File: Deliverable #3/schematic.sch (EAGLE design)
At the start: 61 parts, among them Q1 MMBT4403, Q2 MMBT4403, U1 JOYSTICKPTH, U2 HX711, U3 JOYSTICKPTH, U4 MSP430FR5994IZVW, U5 HX711, U6 VL6180V1NR/1, U7 OSHW-LOGOS

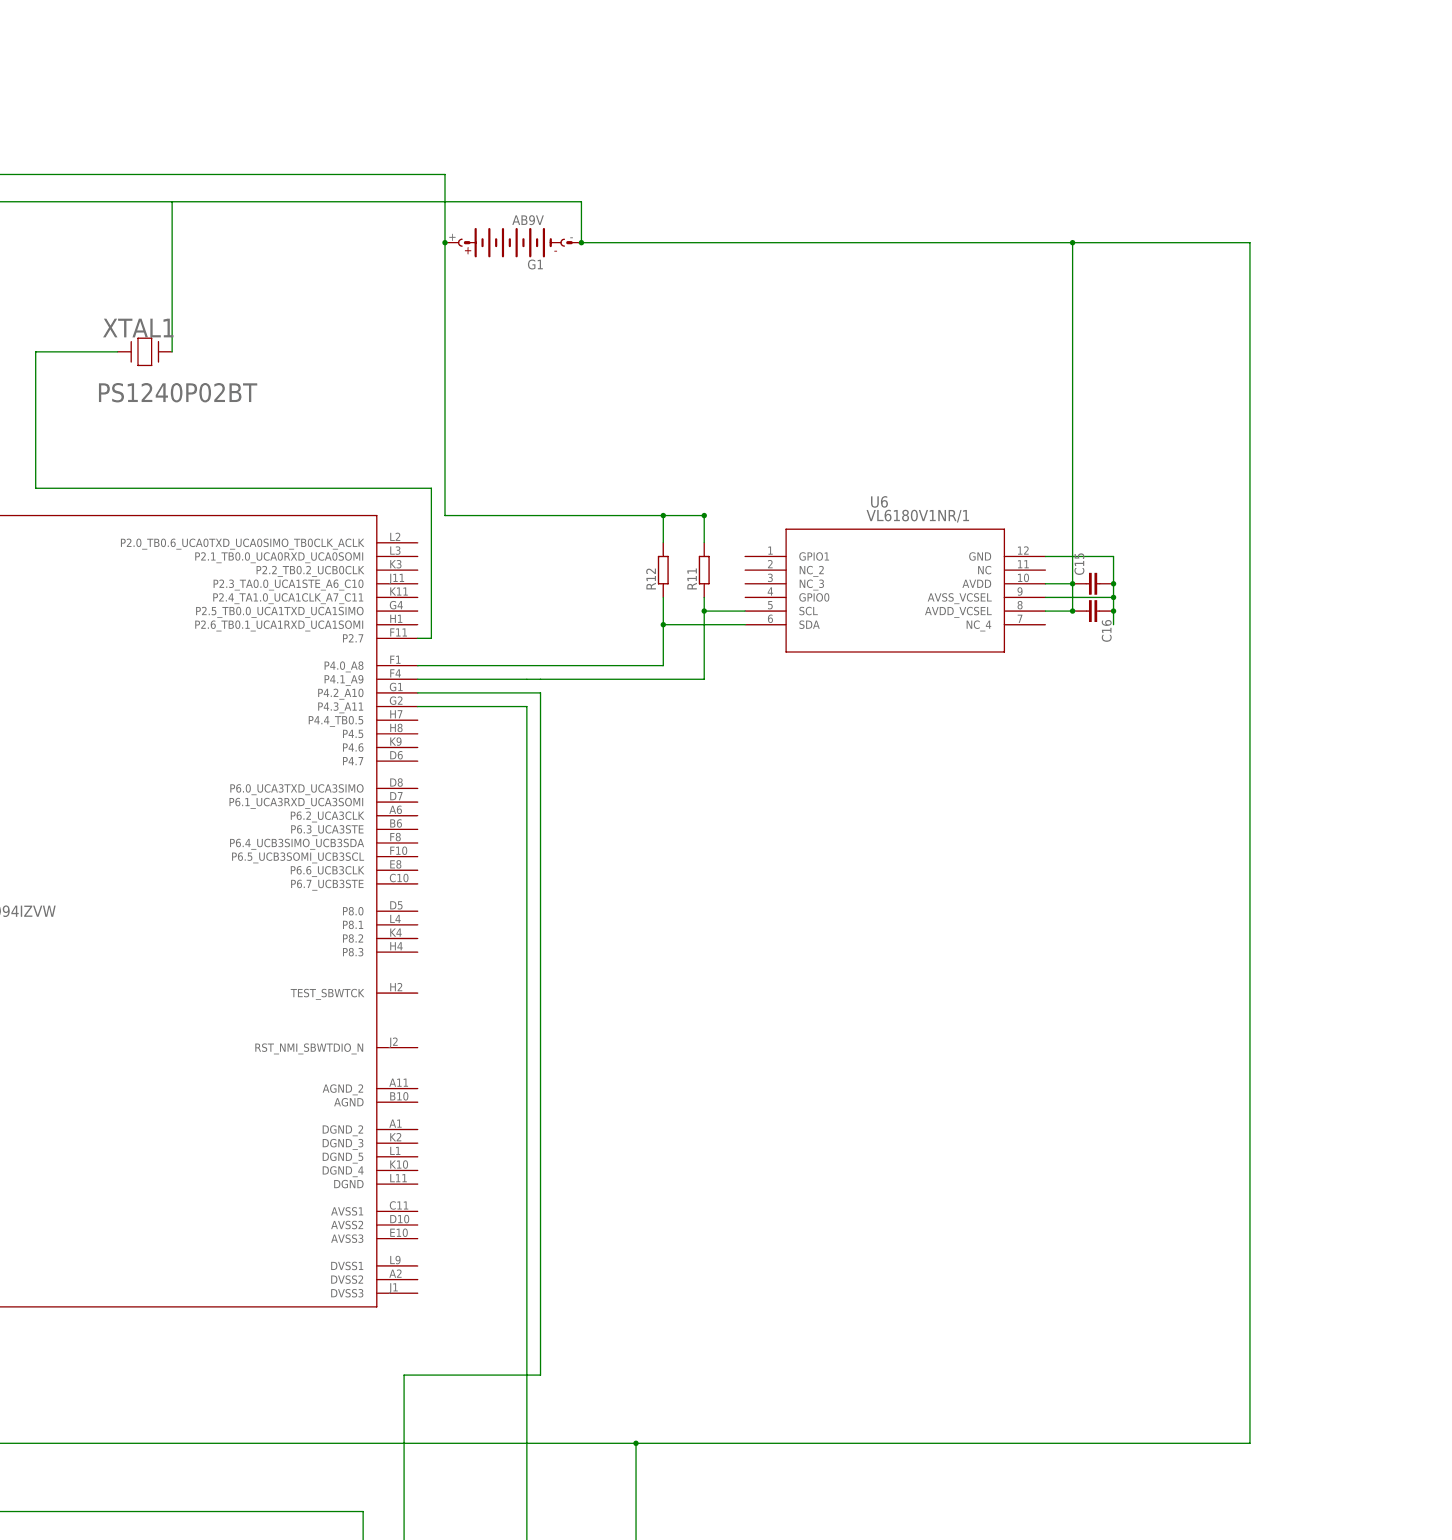
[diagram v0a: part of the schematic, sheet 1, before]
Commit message: added servo to schematic
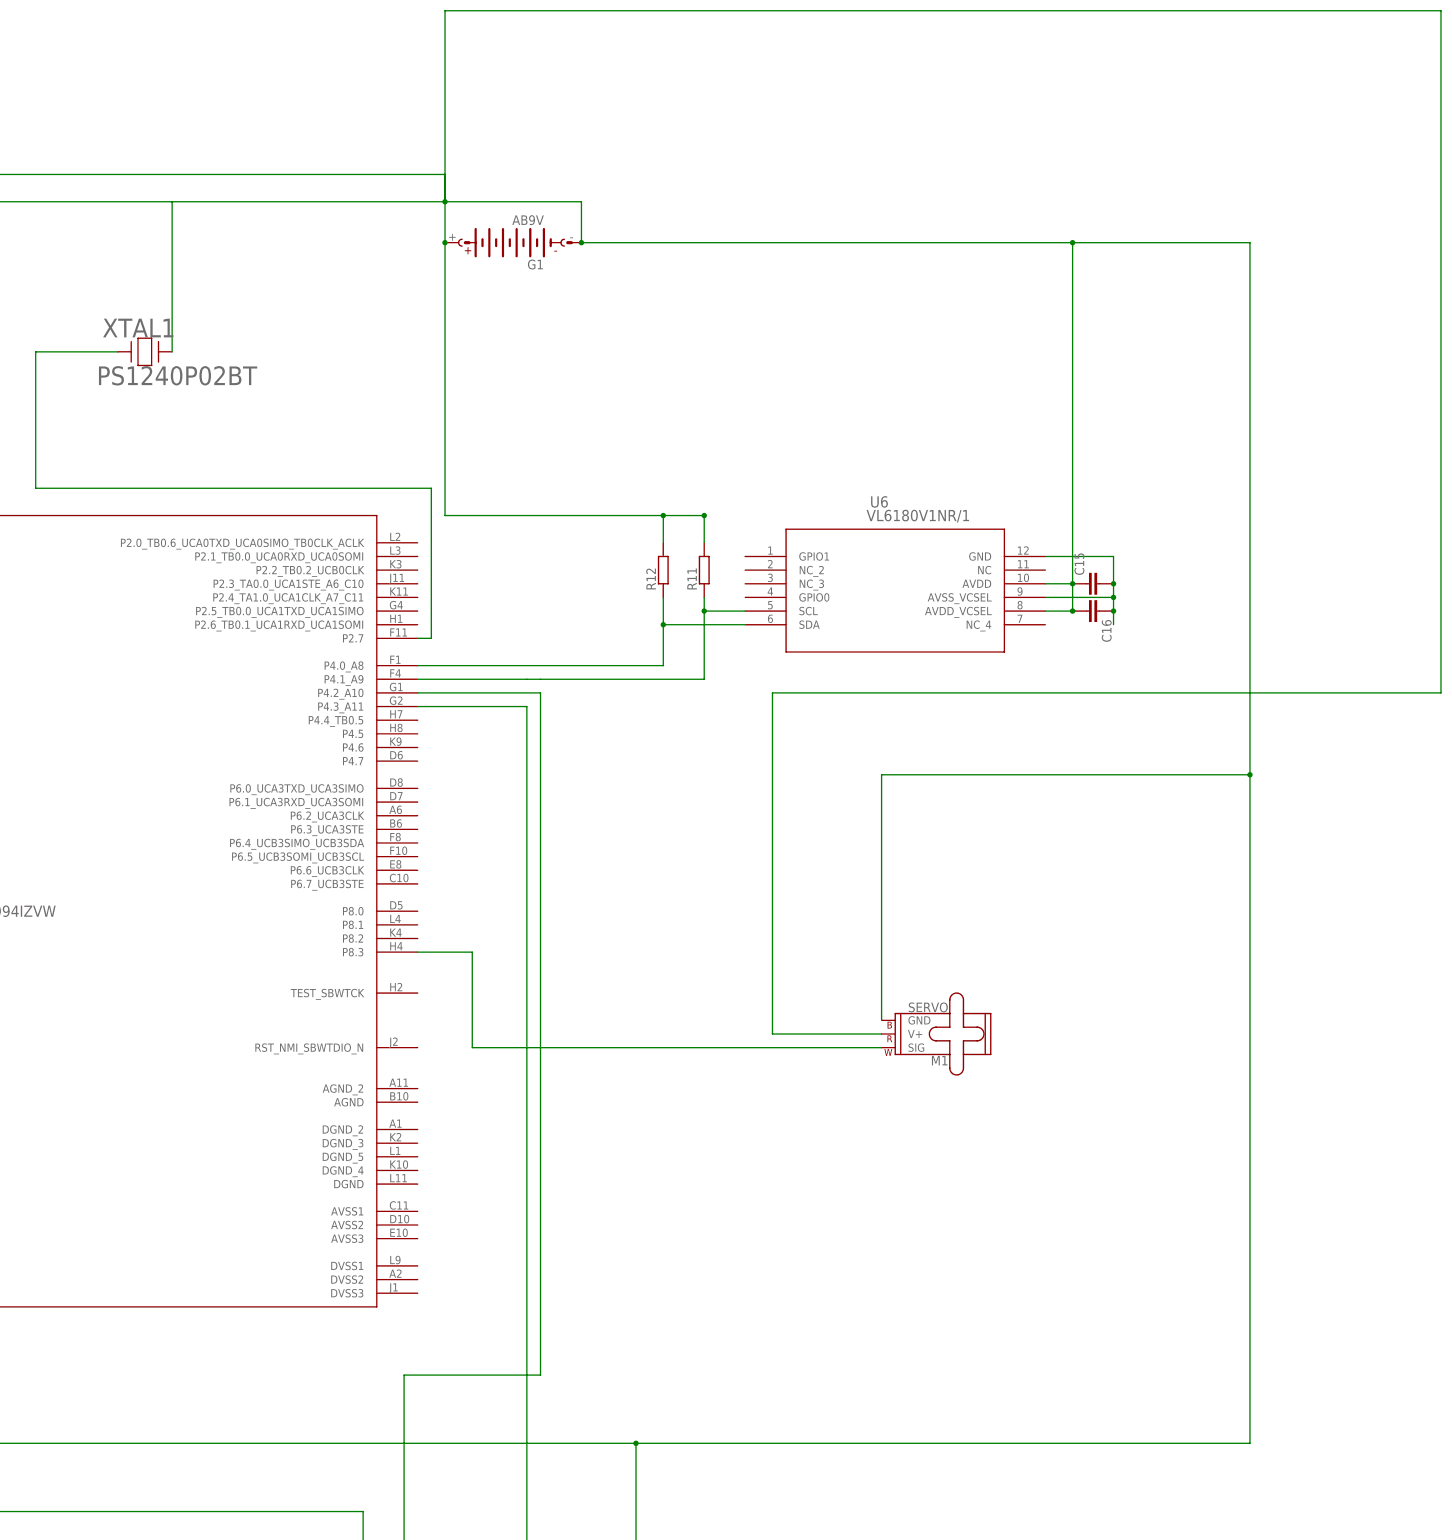
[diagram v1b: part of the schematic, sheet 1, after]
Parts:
- added M1: SERVO, SparkFun-Electromechanical:SERVO
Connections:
- new net N$13: M1.SIG, U4.P8.3
- net GND: now also M1.GND, M1.V+
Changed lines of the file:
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@@
 <layer number="115" name="ReferenceISLANDS" color="7" fill="1" visible="yes" active="yes"/>
 <layer number="116" name="Patch_BOT" color="9" fill="4" visible="yes" active="yes"/>
+<layer number="117" name="PM_Ref" color="26" fill="1" visible="no" active="no"/>
 <layer number="118" name="Rect_Pads" color="7" fill="1" visible="yes" active="yes"/>
+<layer number="119" name="PF_Ref" color="31" fill="1" visible="no" active="no"/>
+<layer number="120" name="WFL_Ref" color="25" fill="1" visible="no" active="no"/>
 <layer number="121" name="_tsilk" color="7" fill="1" visible="yes" active="yes"/>
 <layer number="122" name="_bsilk" color="7" fill="1" visible="yes" active="yes"/>
@@
 <layer number="128" name="_bValues" color="7" fill="1" visible="yes" active="yes"/>
 <layer number="129" name="Mask" color="7" fill="1" visible="yes" active="yes"/>
+<layer number="130" name="SMDSTROOK" color="7" fill="1" visible="no" active="no"/>
 <layer number="131" name="tAdjust" color="7" fill="1" visible="no" active="yes"/>
 <layer number="132" name="bAdjust" color="7" fill="1" visible="no" active="yes"/>
+<layer number="133" name="bottom_silk" color="7" fill="1" visible="no" active="no"/>
+<layer number="134" name="silk_top" color="7" fill="1" visible="no" active="no"/>
+<layer number="135" name="silk_bottom" color="7" fill="1" visible="no" active="no"/>
+<layer number="136" name="silktop" color="7" fill="1" visible="no" active="no"/>
+<layer number="137" name="silkbottom" color="7" fill="1" visible="no" active="no"/>
+<layer number="138" name="EEE" color="7" fill="1" visible="no" active="no"/>
+<layer number="139" name="_tKeepout" color="7" fill="1" visible="no" active="no"/>
+<layer number="140" name="mbKeepout" color="7" fill="1" visible="no" active="no"/>
+<layer number="141" name="ASSEMBLY_TOP" color="7" fill="1" visible="no" active="no"/>
+<layer number="142" name="mbRestrict" color="7" fill="1" visible="no" active="no"/>
+<layer number="143" name="PLACE_BOUND_TOP" color="7" fill="1" visible="no" active="no"/>
 <layer number="144" name="Drill_legend" color="7" fill="1" visible="no" active="yes"/>
+<layer number="145" name="DrillLegend_01-16" color="7" fill="1" visible="no" active="no"/>
+<layer number="146" name="DrillLegend_01-20" color="7" fill="1" visible="no" active="no"/>
+<layer number="147" name="PIN_NUMBER" color="7" fill="1" visible="no" active="no"/>
+<layer number="148" name="DrillLegend_01-20" color="7" fill="1" visible="no" active="no"/>
+<layer number="149" name="DrillLegend_02-15" color="7" fill="1" visible="no" active="no"/>
 <layer number="150" name="Notes" color="7" fill="1" visible="yes" active="yes"/>
 <layer number="151" name="HeatSink" color="7" fill="1" visible="yes" active="yes"/>
@@
 <layer number="154" name="FabDoc2" color="7" fill="1" visible="yes" active="yes"/>
 <layer number="155" name="FabDoc3" color="7" fill="1" visible="yes" active="yes"/>
+<layer number="166" name="AntennaArea" color="7" fill="1" visible="no" active="no"/>
+<layer number="168" name="4mmHeightArea" color="7" fill="1" visible="no" active="no"/>
+<layer number="191" name="mNets" color="7" fill="1" visible="no" active="no"/>
+<layer number="192" name="mBusses" color="7" fill="1" visible="no" active="no"/>
+<layer number="193" name="mPins" color="7" fill="1" visible="no" active="no"/>
+<layer number="194" name="mSymbols" color="7" fill="1" visible="no" active="no"/>
+<layer number="195" name="mNames" color="7" fill="1" visible="no" active="no"/>
+<layer number="196" name="mValues" color="7" fill="1" visible="no" active="no"/>
 <layer number="199" name="Contour" color="7" fill="1" visible="yes" active="yes"/>
 <layer number="200" name="200bmp" color="1" fill="10" visible="yes" active="yes"/>
@@
 <layer number="230" name="230bmp" color="7" fill="1" visible="yes" active="yes"/>
 <layer number="231" name="231bmp" color="7" fill="1" visible="yes" active="yes"/>
+<layer number="232" name="Eagle3D_PG2" color="7" fill="1" visible="no" active="no"/>
+<layer number="233" name="Eagle3D_PG3" color="7" fill="1" visible="no" active="no"/>
 <layer number="248" name="Housing" color="7" fill="1" visible="yes" active="yes"/>
 <layer number="249" name="Edge" color="7" fill="1" visible="yes" active="yes"/>
@@
 <part name="GND20" library="SparkFun-Aesthetics" deviceset="GND" device=""/>
 <part name="C14" library="SparkFun-Capacitors" deviceset="0.1UF-25V-5%(0603)" device="" value="0.1uF"/>
+<part name="M1" library="SparkFun-Electromechanical" deviceset="SERVO" device=""/>
 </parts>
 <sheets>
@@
 <attribute name="NAME" x="190.2206" y="160.1724" size="3.4798" layer="95" ratio="10" rot="SR0"/>
 <attribute name="VALUE" x="189.1538" y="151.2824" size="3.4798" layer="96" ratio="10" rot="SR0"/>
-<attribute name="VALUE" x="189.1538" y="148.1328" size="3.4798" layer="96" ratio="10" rot="SR0"/>
 </instance>
 <instance part="U4" gate="A" x="160.02" y="53.34" smashed="yes">
@@
 <attribute name="NAME" x="125.984" y="-73.279" size="1.778" layer="95"/>
 <attribute name="VALUE" x="125.984" y="-78.359" size="1.778" layer="96"/>
+</instance>
+<instance part="M1" gate="G$1" x="337.82" y="27.94" smashed="yes" rot="R180">
+<attribute name="NAME" x="347.726" y="26.416" size="1.778" layer="95" font="vector" rot="R180"/>
+<attribute name="VALUE" x="347.726" y="34.544" size="1.778" layer="95" font="vector" rot="R180" align="top-left"/>
 </instance>
 </instances>
@@
 <wire x1="63.5" y1="-45.72" x2="289.56" y2="-45.72" width="0.1524" layer="91"/>
 <wire x1="289.56" y1="-45.72" x2="403.86" y2="-45.72" width="0.1524" layer="91"/>
-<wire x1="403.86" y1="-45.72" x2="403.86" y2="177.8" width="0.1524" layer="91"/>
+<wire x1="403.86" y1="-45.72" x2="403.86" y2="78.74" width="0.1524" layer="91"/>
+<wire x1="403.86" y1="78.74" x2="403.86" y2="177.8" width="0.1524" layer="91"/>
 <wire x1="38.1" y1="60.96" x2="35.56" y2="60.96" width="0.1524" layer="91"/>
 <wire x1="35.56" y1="60.96" x2="35.56" y2="50.8" width="0.1524" layer="91"/>
@@
 <junction x="279.4" y="177.8"/>
 <pinref part="XTAL1" gate="A" pin="2"/>
-<wire x1="279.4" y1="185.42" x2="203.2" y2="185.42" width="0.1524" layer="91"/>
+<wire x1="279.4" y1="185.42" x2="254" y2="185.42" width="0.1524" layer="91"/>
+<wire x1="254" y1="185.42" x2="203.2" y2="185.42" width="0.1524" layer="91"/>
 <wire x1="203.2" y1="185.42" x2="203.2" y2="157.48" width="0.1524" layer="91"/>
 <wire x1="-7.62" y1="50.8" x2="-7.62" y2="185.42" width="0.1524" layer="91"/>
@@
 <wire x1="289.56" y1="-134.62" x2="289.56" y2="-45.72" width="0.1524" layer="91"/>
 <junction x="289.56" y="-45.72"/>
+<pinref part="M1" gate="G$1" pin="GND"/>
+<wire x1="335.28" y1="33.02" x2="335.28" y2="78.74" width="0.1524" layer="91"/>
+<wire x1="335.28" y1="78.74" x2="403.86" y2="78.74" width="0.1524" layer="91"/>
+<junction x="403.86" y="78.74"/>
+<pinref part="M1" gate="G$1" pin="V+"/>
+<wire x1="335.28" y1="30.48" x2="314.96" y2="30.48" width="0.1524" layer="91"/>
+<wire x1="314.96" y1="30.48" x2="314.96" y2="93.98" width="0.1524" layer="91"/>
+<wire x1="314.96" y1="93.98" x2="439.42" y2="93.98" width="0.1524" layer="91"/>
+<wire x1="439.42" y1="93.98" x2="439.42" y2="220.98" width="0.1524" layer="91"/>
+<wire x1="439.42" y1="220.98" x2="254" y2="220.98" width="0.1524" layer="91"/>
+<wire x1="254" y1="220.98" x2="254" y2="185.42" width="0.1524" layer="91"/>
+<junction x="254" y="185.42"/>
 </segment>
 <segment>
@@
 </segment>
 </net>
+<net name="N$13" class="0">
+<segment>
+<pinref part="M1" gate="G$1" pin="SIG"/>
+<wire x1="335.28" y1="27.94" x2="259.08" y2="27.94" width="0.1524" layer="91"/>
+<wire x1="259.08" y1="27.94" x2="259.08" y2="45.72" width="0.1524" layer="91"/>
+<pinref part="U4" gate="A" pin="P8.3"/>
+<wire x1="259.08" y1="45.72" x2="248.92" y2="45.72" width="0.1524" layer="91"/>
+</segment>
+</net>
